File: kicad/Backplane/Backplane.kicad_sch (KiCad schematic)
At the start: 71 parts, among them J1 Control Connector, J10 I/O Connector, J11 I/O Connector, J12 I/O Connector, J13 I/O Connector, J14 I/O Connector, J15 Front Panel Connector, J16 Front Panel Connector, J17 Run, J18 Clock, J19 Rept, J2 Data Connector, J20 Reset, J21 I/O Reset, J3 Control Connector, J4 Data Connector, J5 Control Connector, J6 Data Connector, J7 Control Connector, J8 Data Connector, J9 I/O Connector, U1 74LS244, U10 74LS377, U11 74LS377, U12 74LS377, U13 74LS244, U14 74LS244, U15 74LS244, U16 74LS04, U17 74LS244, U18 74LS244, U19 74LS244, U2 74LS244, U20 74LS377, U21 74LS148, U22 74LS153, U3 74LS74, U4 74LS74, U5 74LS32, U6 74LS08, U7 74LS245, U8 74LS245, U9 74LS245, X1 4 Mhz Oscillator

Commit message: Switch out to 74LS253
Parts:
- removed U22: 74LS153, symbol 74xx:74LS153
- added U22: 74LS253, symbol 74xx:74LS253
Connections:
- net *CHAN_REQ: now also U22.7 (Za)
- net *DMA_REQ: now also U22.9 (Zb)
- net +5V: now also U22.16 (VCC)
- net GND: now also U22.1 (OEa), U22.15 (OEb), U22.8 (GND)
- net at U20.16 (Q6), U21.3 (I6): now also U22.10 (I0b)
- net at U20.12 (Q4), U21.1 (I4): now also U22.11 (I1b)
- net at U20.6 (Q2), U21.12 (I2): now also U22.12 (I2b)
- net at U20.2 (Q0), U21.10 (IO): now also U22.13 (I3b)
- net at U21.7 (S1): now also U22.14 (A0)
- net at U21.6 (S2): now also U22.2 (A1)
- net at U20.5 (Q1), U21.11 (I1): now also U22.3 (I3a)
- net at U20.9 (Q3), U21.13 (I3): now also U22.4 (I2a)
- net at U20.15 (Q5), U21.2 (I5): now also U22.5 (I1a)
- net at U20.19 (Q7), U21.4 (I7): now also U22.6 (I0a)
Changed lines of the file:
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@@
-    )
-  )
-  (symbol (lib_id "74xx:74LS153") (at 434.975 274.32 0) (unit 1)
-    (in_bom yes) (on_board yes) (dnp no) (fields_autoplaced)
-    (property "Reference" "U22" (at 437.1691 249.8557 0)
-      (effects (font (size 1.27 1.27)) (justify left))
-    )
-    (property "Value" "74LS153" (at 437.1691 252.2799 0)
-      (effects (font (size 1.27 1.27)) (justify left))
-    )
-    (property "Footprint" "" (at 434.975 274.32 0)
-      (effects (font (size 1.27 1.27)) hide)
-    )
-    (property "Datasheet" "http://www.ti.com/lit/gpn/sn74LS153" (at 434.975 274.32 0)
-      (effects (font (size 1.27 1.27)) hide)
-    )
-    (pin "1")
-    (pin "10")
-    (pin "11")
-    (pin "12")
-    (pin "13")
-    (pin "14")
-    (pin "15")
-    (pin "16")
-    (pin "2")
-    (pin "3")
-    (pin "4")
-    (pin "5")
-    (pin "6")
-    (pin "7")
-    (pin "8")
-    (pin "9")
-    (instances
-      (project "Backplane"
-        (path "/44159f72-1097-48fe-bad4-abb772ed1b2f"
-          (reference "U22") (unit 1)
-        )
-      )
     )
   )
@@
         )
       )
+    )
+  )
+  (symbol (lib_id "74xx:74LS253") (at 434.975 274.32 0) (unit 1)
+    (in_bom yes) (on_board yes) (dnp no) (fields_autoplaced)
+    (property "Reference" "U22" (at 437.1691 249.8557 0)
+      (effects (font (size 1.27 1.27)) (justify left))
+    )
+    (property "Value" "74LS253" (at 437.1691 252.2799 0)
+      (effects (font (size 1.27 1.27)) (justify left))
+    )
+    (property "Footprint" "" (at 434.975 274.32 0)
+      (effects (font (size 1.27 1.27)) hide)
+    )
+    (property "Datasheet" "http://www.ti.com/lit/gpn/sn74LS253" (at 434.975 274.32 0)
+      (effects (font (size 1.27 1.27)) hide)
+    )
+    (pin "1")
+    (pin "10")
+    (pin "11")
+    (pin "12")
+    (pin "13")
+    (pin "14")
+    (pin "15")
+    (pin "16")
+    (pin "2")
+    (pin "3")
+    (pin "4")
+    (pin "5")
+    (pin "6")
+    (pin "7")
+    (pin "8")
+    (pin "9")
+    (instances
+      (project "Backplane"
+        (path "/44159f72-1097-48fe-bad4-abb772ed1b2f"
+          (reference "U22") (unit 1)
+        )
+      )

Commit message: Continue work on backplane schematic
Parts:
- added C1, C10, C11, C12, C13, C14, C15, C16, C17, C18, C19, C2, C20, C21, C22, C23, C24, C25, C3, C4, C5, C6, C7, C8, C9: 0.1uF, symbol Device:C
- added C20: 100 uF, Capacitor_THT:CP_Radial_D6.3mm_P2.50mm, symbol Device:C_Polarized
- added R28, R29, R30, R31, R32, R33, R34, R35, R36, R37, R38, R39, R40, R41, R42, R43, R44, R45, R46, R47, R48, R49, R50, R51, R52, R53: 4.7K, Resistor_THT:R_Axial_DIN0207_L6.3mm_D2.5mm_P7.62mm_Horizontal, symbol Device:R
- added U23: 74LS139, symbol 74xx:74LS139
- added U24: 74LS244, symbol 74xx:74LS244
- added U25: 74LS32, symbol 74xx:74LS32
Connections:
- net *CHAN_REQ: now also R28.2
- net *CHAN_REQ0: now also R47.1
- net *CHAN_REQ1: now also R49.1
- net *CHAN_REQ2: now also R51.1
- net *CHAN_REQ3: now also R53.1
- net *DEV_REQ: now also U21.14 (GS), R34.1
- net *DMA_REQ: now also R29.1
- net *DMA_REQ0: now also R46.1
- net *DMA_REQ1: now also R48.1
- net *DMA_REQ2: now also R50.1
- net *DMA_REQ3: now also R52.1
- net *DRQ_GRANT: now also U23.1 (E)
- net *DRQ_GRANT0: now also U23.4 (O0)
- net *DRQ_GRANT1: now also U23.5 (O1)
- net *DRQ_GRANT2: now also U23.6 (O2)
- net *DRQ_GRANT3: now also U23.7 (O3)
- net *INCREMENT_ZERO: now also U16.8
- net *INT_REQ: now also R35.1
- net *IORS_FLAG0: now also R38.1
- net *IORS_FLAG1: now also R39.1
- net *IORS_FLAG2: now also R40.1
- net *IORS_FLAG3: now also R41.1
- net *IOT_SKIP: now also R36.1
- net *IOT_WAIT: now also R37.1
- net *MEMM_ENABLE: now also R31.1
- net *PI_ENABLE: now also R30.1
- net *PROT_ENABLE: now also R32.1; no longer J10.b24 (Pin_b24), J11.b24 (Pin_b24), J12.b24 (Pin_b24), J13.b24 (Pin_b24), J14.b24 (Pin_b24), J9.b24 (Pin_b24)
- net *PTP_FLAG: now also R43.1
- net *PTP_TAPE: now also R45.1
- net *PTR_FLAG: now also R42.1
- net *PTR_TAPE: now also R44.1
- net *RESET: now also U5.11; no longer U6.8
- net *REST_PEND: now also J10.b24 (Pin_b24), J11.b24 (Pin_b24), J12.b24 (Pin_b24), J13.b24 (Pin_b24), J14.b24 (Pin_b24), J9.b24 (Pin_b24), R33.1
- net +5V: now also U16.14 (VCC), U3.14 (VCC), U4.14 (VCC), U5.14 (VCC), U6.14 (VCC), C1.1, C10.1, C11.1, C12.1, C13.1, C14.1, C15.1, C16.1, C17.1, C18.1, C19.1, C2.1, C20.1, C20.1, C21.1, C22.1, C23.1, C24.1, C25.1, C3.1, C4.1, C5.1, C6.1, C7.1, C8.1, C9.1, R28.1, R29.2, R30.2, R31.2, R32.2, R33.2, R34.2, R35.2, R36.2, R37.2, R38.2, R39.2, R40.2, R41.2, R42.2, R43.2, R44.2, R45.2, R46.2, R47.2, R48.2, R49.2, R50.2, R51.2, R52.2, R53.2, U23.16 (VCC), U24.20 (VCC), U25.14 (VCC)
- net A0: now also U25.1, U25.2
- net A1: now also U25.4, U25.5
- net A10: now also U24.15 (I2b)
- net A11: now also U24.17 (I3b)
- net A2: now also U25.10, U25.9
- net A4: now also U24.2 (I0a)
- net A5: now also U24.4 (I1a)
- net A6: now also U24.6 (I2a)
- net A7: now also U24.8 (I3a)
- net A8: now also U24.11 (I0b)
- net A9: now also U24.13 (I1b)
- net A_DEVICE0: now also U24.14 (O2a)
- net A_DEVICE1: now also U24.12 (O3a)
- net A_DEVICE2: now also U24.9 (O0b)
- net A_DEVICE3: now also U24.7 (O1b)
- net A_DEVICE4: now also U24.5 (O2b)
- net A_DEVICE5: now also U24.3 (O3b)
- net A_PULSE0: now also U25.3
- net A_PULSE1: now also U25.6
- net A_PULSE2: now also U25.8
- net A_SUBDEV0: now also U24.18 (O0a)
- net A_SUBDEV1: now also U24.16 (O1a)
- net CTL_CONST: now also U6.9
- net D0: now also U17.18 (O0a); no longer U17.2 (I0a)
- net D1: now also U17.16 (O1a); no longer U17.4 (I1a)
- net D10: now also U18.14 (O2a); no longer U18.6 (I2a)
- net D11: now also U18.12 (O3a); no longer U18.8 (I3a)
- net D12: now also U18.9 (O0b); no longer U18.11 (I0b)
- net D13: now also U18.7 (O1b); no longer U18.13 (I1b)
- net D14: now also U18.5 (O2b); no longer U18.15 (I2b)
- net D15: now also U18.3 (O3b); no longer U18.17 (I3b)
- net D16: now also U19.18 (O0a); no longer U19.2 (I0a)
- net D17: now also U19.16 (O1a); no longer U19.4 (I1a)
- net D2: now also U17.14 (O2a); no longer U17.6 (I2a)
- net D3: now also U17.12 (O3a); no longer U17.8 (I3a)
- net D4: now also U17.9 (O0b); no longer U17.11 (I0b)
- net D5: now also U17.7 (O1b); no longer U17.13 (I1b)
- net D6: now also U17.5 (O2b); no longer U17.15 (I2b)
- net D7: now also U17.3 (O3b); no longer U17.17 (I3b)
- net D8: now also U18.18 (O0a); no longer U18.2 (I0a)
- net D9: now also U18.16 (O1a); no longer U18.4 (I1a)
- net FLAG_ZERO: now also U6.10
- net GND: now also U16.11, U16.13, U16.7 (GND), U19.11 (I0b), U19.13 (I1b), U19.15 (I2b), U19.17 (I3b), U19.6 (I2a), U19.8 (I3a), U3.7 (GND), U4.7 (GND), U5.7 (GND), U6.7 (GND), C1.2, C10.2, C11.2, C12.2, C13.2, C14.2, C15.2, C16.2, C17.2, C18.2, C19.2, C2.2, C20.2, C20.2, C21.2, C22.2, C23.2, C24.2, C25.2, C3.2, C4.2, C5.2, C6.2, C7.2, C8.2, C9.2, U23.13 (A1), U23.14 (A0), U23.15 (E), U23.8 (GND), U24.1 (OEa), U24.10 (GND), U24.19 (OEb), U25.12, U25.13, U25.7 (GND); no longer U19.12 (O3a), U19.14 (O2a), U19.3 (O3b), U19.5 (O2b), U19.7 (O1b), U19.9 (O0b)
- net ID0: now also U17.2 (I0a); no longer U17.18 (O0a)
- net ID1: now also U17.4 (I1a); no longer U17.16 (O1a)
- net ID10: now also U18.6 (I2a); no longer U18.14 (O2a)
- net ID11: now also U18.8 (I3a); no longer U18.12 (O3a)
- net ID12: now also U18.11 (I0b); no longer U18.9 (O0b)
- net ID13: now also U18.13 (I1b); no longer U18.7 (O1b)
- net ID14: now also U18.15 (I2b); no longer U18.5 (O2b)
- net ID15: now also U18.17 (I3b); no longer U18.3 (O3b)
- net ID16: now also U19.2 (I0a); no longer U19.18 (O0a)
- net ID17: now also U19.4 (I1a); no longer U19.16 (O1a)
- net ID2: now also U17.6 (I2a); no longer U17.14 (O2a)
- net ID3: now also U17.8 (I3a); no longer U17.12 (O3a)
- net ID4: now also U17.11 (I0b); no longer U17.9 (O0b)
- net ID5: now also U17.13 (I1b); no longer U17.7 (O1b)
- net ID6: now also U17.15 (I2b); no longer U17.5 (O2b)
- net ID7: now also U17.17 (I3b); no longer U17.3 (O3b)
- net ID8: now also U18.2 (I0a); no longer U18.18 (O0a)
- net ID9: now also U18.4 (I1a); no longer U18.16 (O1a)
- net at U21.7 (S1), U22.14 (A0): now also U23.2 (A0)
- net at U21.6 (S2), U22.2 (A1): now also U23.3 (A1)
- net at U16.9: now also U6.8
- net at J20.2 (Pin_2), R4.1: now also U5.12, U5.13; no longer U6.10, U6.9
- no-connect marks 68 -> 75
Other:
- moved on the sheet: R27, U16A, U16C, U16D, U16E, U16F, U16G, U4C, U5C, U5D, U5E, U6C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

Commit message: Start laying out backplane
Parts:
- added J22: Power, Connector_TE-Connectivity:TE_MATE-N-LOK_350211-1_1x04_P5.08mm_Vertical, symbol Connector_Generic:Conn_01x04
- added J23: Power LED, Connector_PinHeader_2.54mm:PinHeader_1x02_P2.54mm_Vertical, symbol Connector:Conn_01x02_Pin
- added R54: 330R, Resistor_THT:R_Axial_DIN0207_L6.3mm_D2.5mm_P7.62mm_Horizontal, symbol Device:R
- C1, C10, C11, C12, C13, C14, C15, C16, C17, C18, C19, C2, C20, C21, C22, C23, C24, C25, C3, C4, C5, C6, C7, C8, C9: footprint (none) -> Capacitor_THT:C_Disc_D5.0mm_W2.5mm_P5.00mm
- J1, J10, J11, J12, J13, J14, J2, J3, J4, J5, J6, J7, J8, J9: footprint Connector_DIN:DIN41612_B_2x32_Male_Horizontal_THT -> Connector_DIN:DIN41612_B_2x32_Female_Vertical_THT
- J17, J18, J19, J20, J21: footprint (none) -> Connector_PinHeader_2.54mm:PinHeader_1x02_P2.54mm_Vertical
- U1, U10, U11, U12, U13, U14, U15, U17, U18, U19, U2, U20, U24, U7, U8, U9: footprint (none) -> Package_DIP:DIP-20_W7.62mm
- U16, U25, U3, U4, U5, U6: footprint (none) -> Package_DIP:DIP-14_W7.62mm
- U21, U22, U23: footprint (none) -> Package_DIP:DIP-16_W7.62mm
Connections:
- net +5V: now also J22.4 (Pin_4), R54.1
- net GND: now also J22.2 (Pin_2), J22.3 (Pin_3), J23.1 (Pin_1)
- net +12V: now reaches J13.b31 (Pin_b31)
- net +12V: now also J10.b31 (Pin_b31), J11.b31 (Pin_b31), J12.b31 (Pin_b31), J14.b31 (Pin_b31), J9.b31 (Pin_b31), J22.1 (Pin_1)
- new net: J23.2 (Pin_2), R54.2
- no-connect marks 75 -> 69

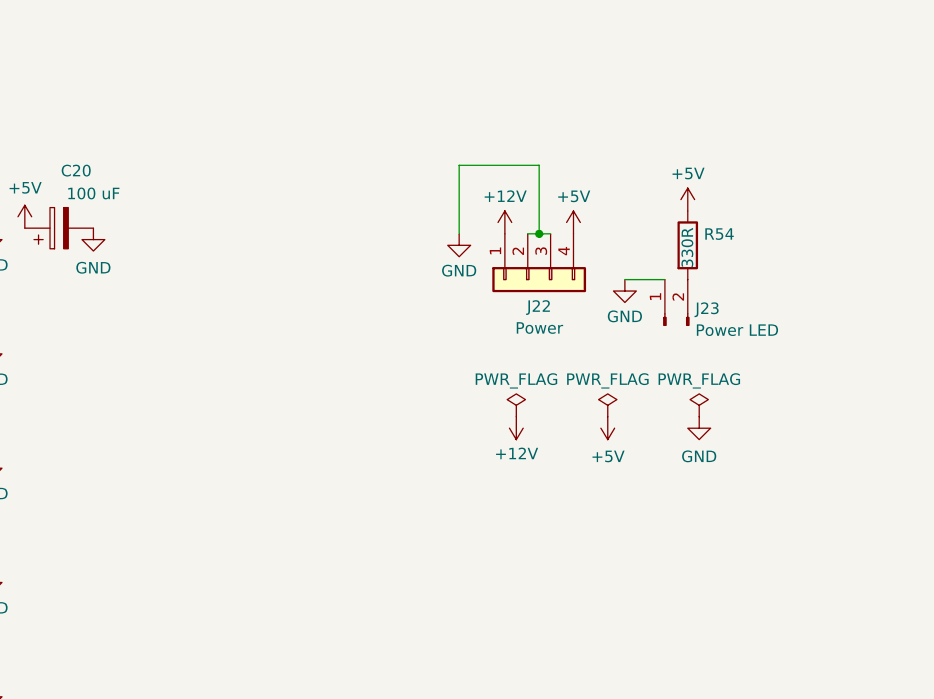
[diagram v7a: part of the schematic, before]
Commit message: Route address front panel
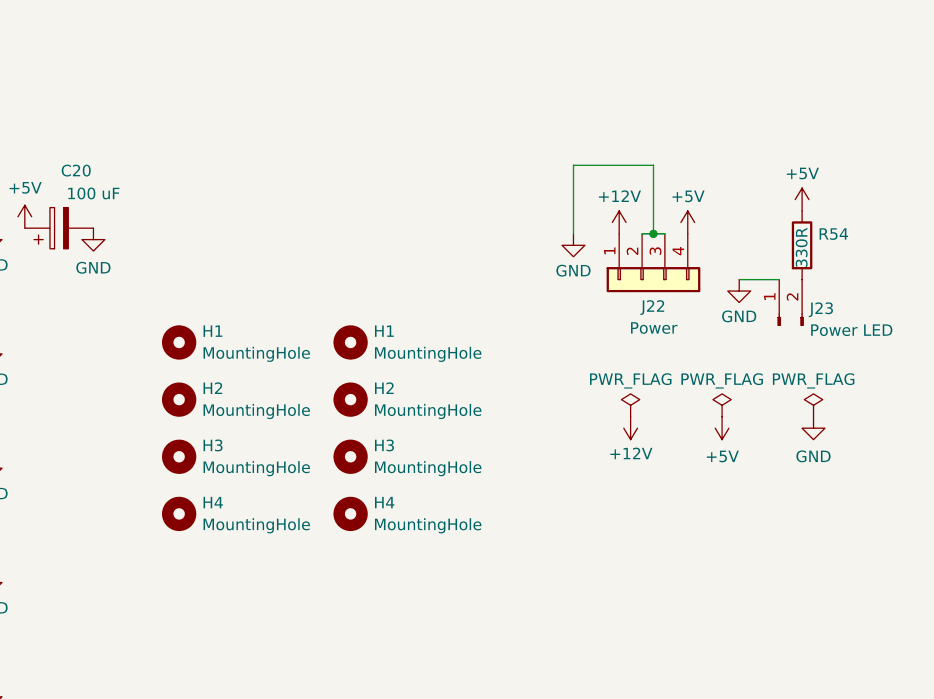
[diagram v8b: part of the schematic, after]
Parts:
- added H1 (x2), H2 (x2), H3 (x2), H4 (x2): MountingHole, MountingHole:MountingHole_2.2mm_M2_Pad, symbol Mechanical:MountingHole
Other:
- moved on the sheet: J22, J23, R54
